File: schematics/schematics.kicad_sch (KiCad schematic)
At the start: 18 parts, among them M1 Motor_Servo, SW1 Reset, U1 74ACT244, U15 Dist_SW, U16 Branch_Slide, U2 RGB_Strip, U3 Distance_Sensor, U4 PIC32MX170F256B

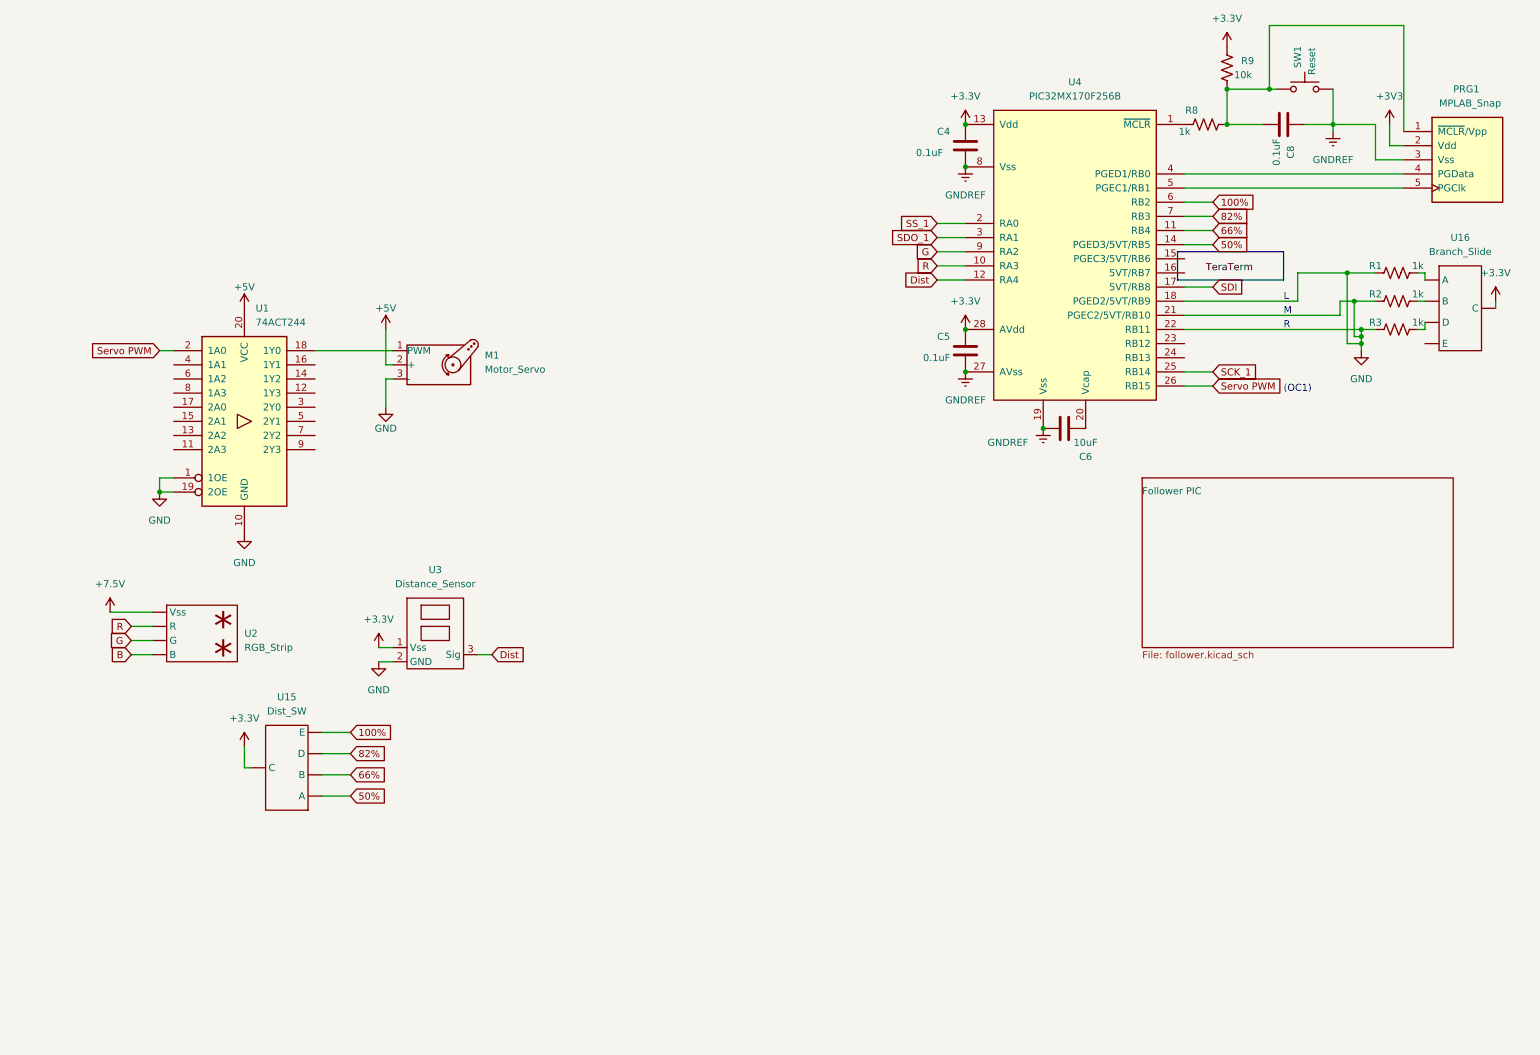
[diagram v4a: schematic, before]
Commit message: Update KiCAD schematic and write getter functions for switches
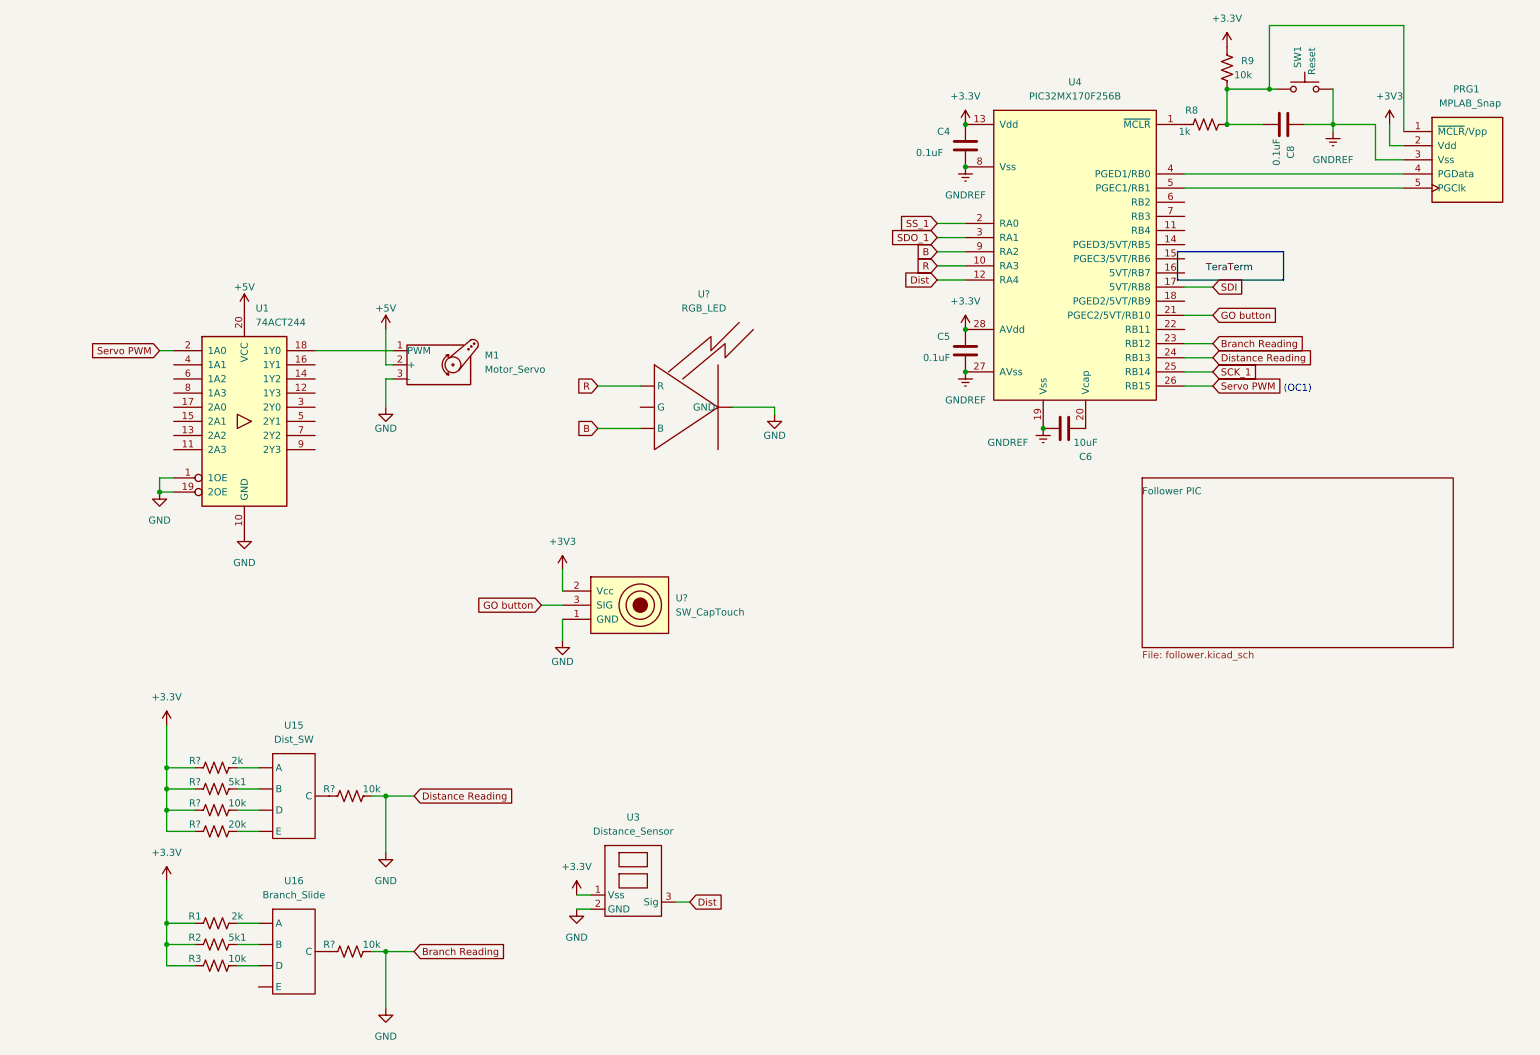
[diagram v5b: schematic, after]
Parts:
- removed U2: RGB_Strip, symbol Custom_Library:RGB_Strip
- added R? (x3): 10k, symbol 218 spdl:Res1
- added R?: 2k, symbol 218 spdl:Res1
- added R?: 5k1, symbol 218 spdl:Res1
- added R?: 20k, symbol 218 spdl:Res1
- added U?: RGB_LED, symbol custom:RGB_LED
- added U?: SW_CapTouch, symbol 218 spdl:SW_CapTouch
- R1: value 1k -> 2k
- R2: value 1k -> 5k1
- R3: value 1k -> 10k
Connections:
- net G is gone; now on net B: U4.9 (RA2)
- net +3.3V: now also R1.1, R2.1, R3.1, R?.1, R?.1, R?.1, R?.1; no longer U15. (E), U16. (E)
- net +3V3: now also U?.2 (Vcc)
- net B: now also U?. (R)
- net GND: now also U4.23 (RB12), U4.24 (RB13), R?.2, R?.2, U?. (R), U?.1 (GND); no longer R1.1, R2.1, R3.1, U4.18 (PGED2/5VT/RB9), U4.21 (PGEC2/5VT/RB10), U4.22 (RB11)
- net R: now also U?. (R)
- net 100%: no longer names the net of U4.6 (RB2)
- net 100%: no longer U15. (E)
- net 50%: no longer names the net of U4.14 (PGED3/5VT/RB5)
- net 50%: no longer U15. (E)
- net 66%: no longer names the net of U4.11 (RB4)
- net 66%: no longer U15. (E)
- net 82%: no longer names the net of U4.7 (RB3)
- net 82%: no longer U15. (E)
- new net: R?.1, U15. (E)
- new net: R?.1, U16. (E)
- new net: R?.2, U15. (E) (x4)
- new net GO button: U4.21 (PGEC2/5VT/RB10), U?.3 (SIG)
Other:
- note removed: "L"
- note removed: "M"
- note removed: "R"
- moved on the sheet: R1, R2, R3, U15, U16, U3
